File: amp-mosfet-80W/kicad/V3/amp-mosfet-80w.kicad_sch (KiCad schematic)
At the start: 66 parts, among them J1 Conn_01x01, J2 Conn_01x01, J3 +50V, J4 -50V, J5 LS+, J6 LS-, J7 GND, Q1 BC856BS, Q11 ECX10P20, Q12 ECX10N20, Q2 BC856BS, Q3 BC856BS, Q4 BC846BDW1, Q5 DZT5401, Q6 DZT5551, Q7 BC856B, Q8 BC846

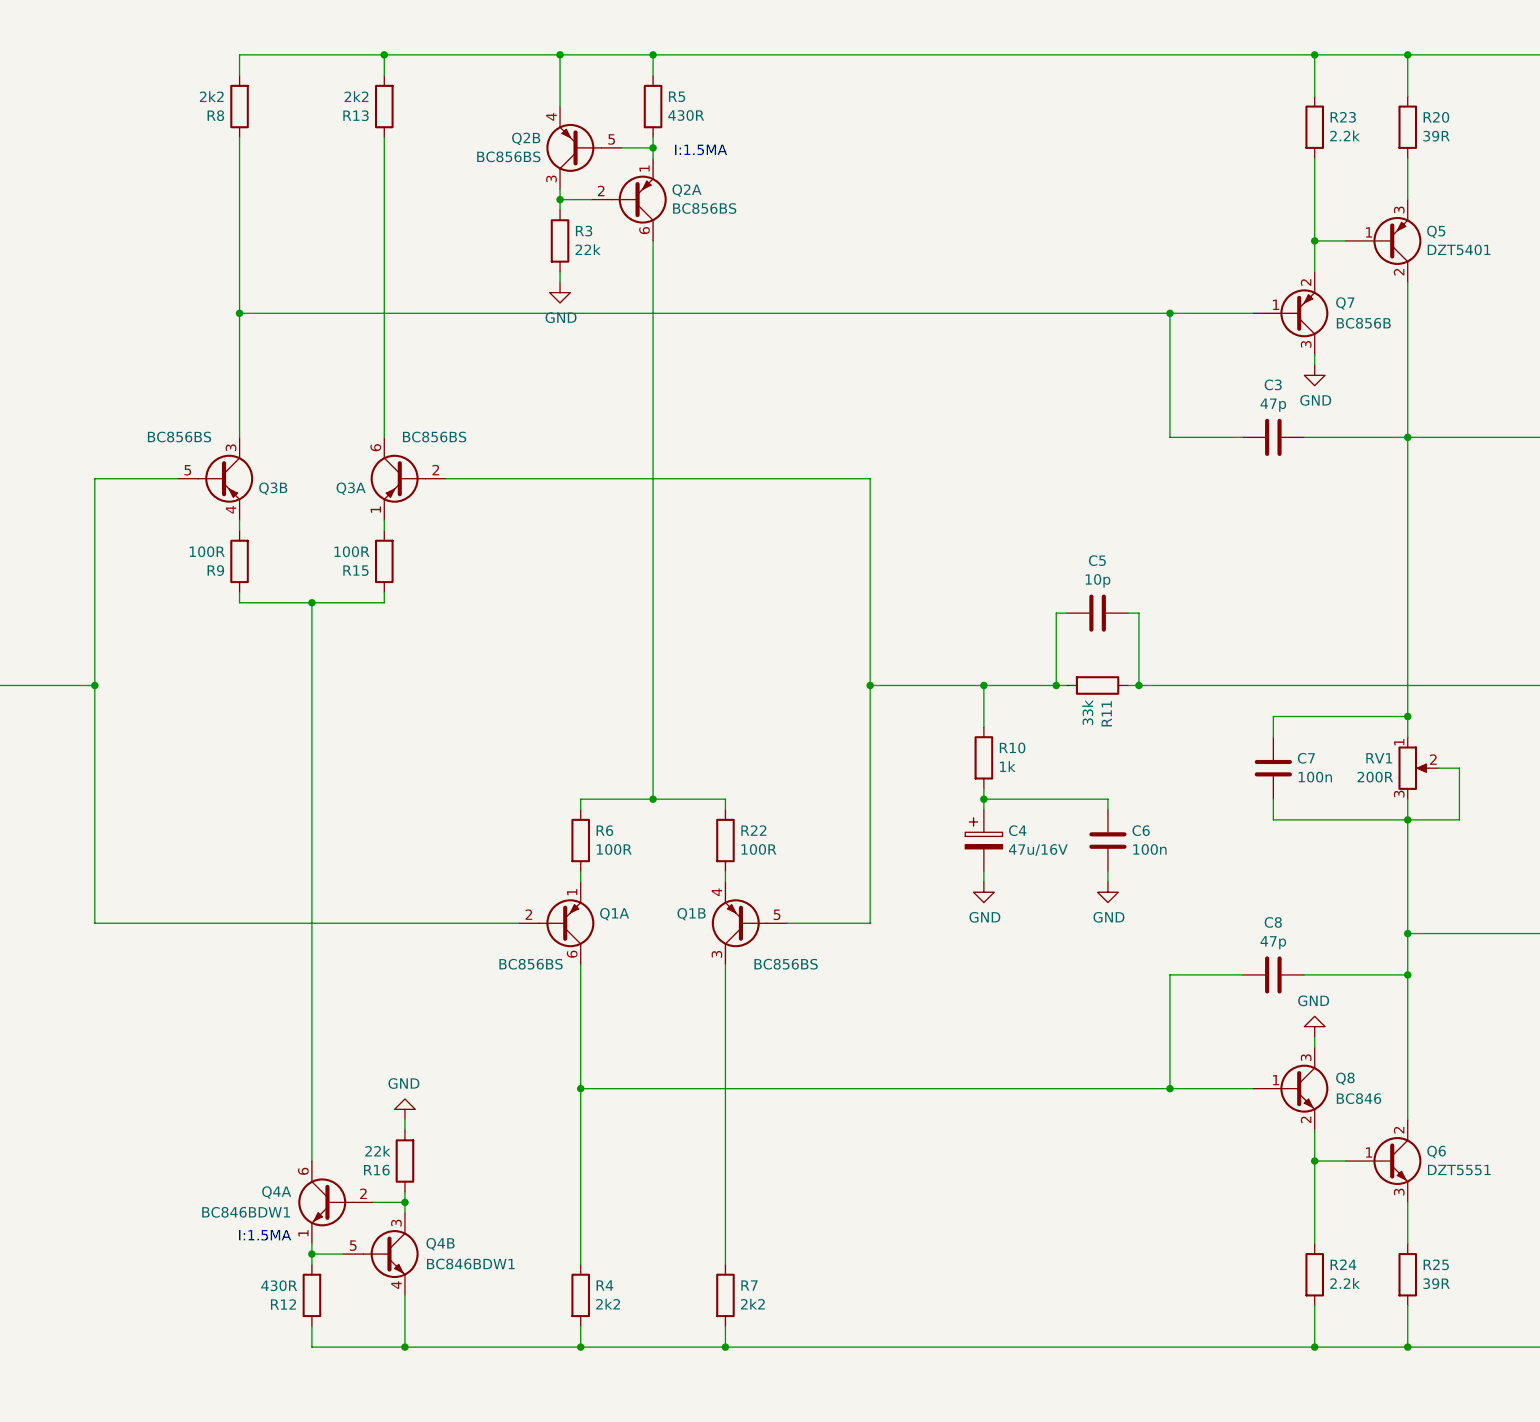
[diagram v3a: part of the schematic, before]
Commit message: Update amp-mosfet-80w.kicad_sch
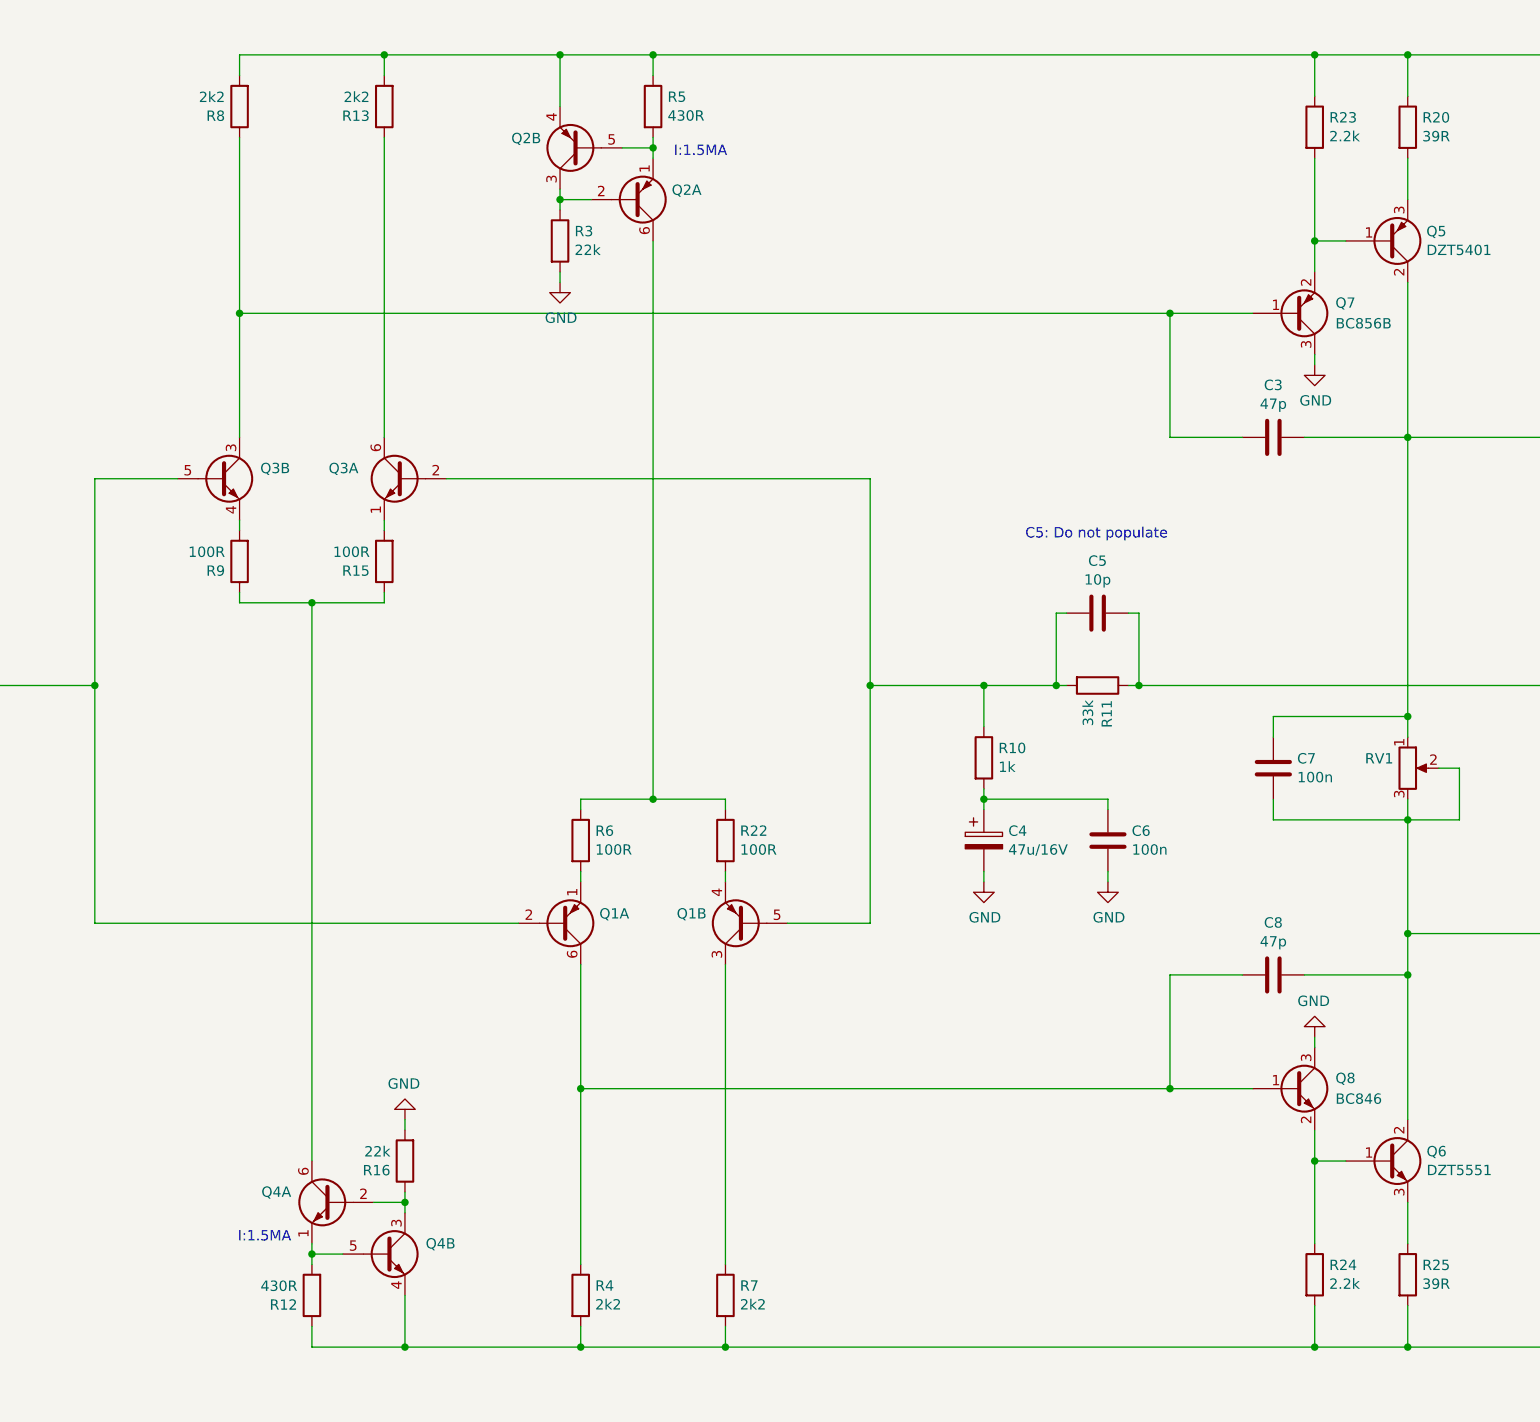
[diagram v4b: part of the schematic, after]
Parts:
- removed Q3: BC856BS, Package_TO_SOT_SMD:SOT-363_SC-70-6, symbol Transistor_BJT:BC856BS
- added Q3: (no value), Package_TO_SOT_SMD:SOT-363_SC-70-6, symbol Transistor_BJT:BC846BDW1
- Q1, Q2: value BC856BS -> (none)
- Q4: value BC846BDW1 -> (none)
- RV1: value 200R -> (none)
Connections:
- net at C2.1, Q1.2 (B1), R2.1: now also Q3.5 (B2)
- net at C5.2, Q1.5 (B2), R10.1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: now also Q3.2 (B1)
- net at R15.2: now also Q3.1 (E1)
- net at R13.1: now also Q3.6 (C1)
- net at C3.2, Q7.1 (B), R8.1: now also Q3.3 (C2)
- net at R9.2: now also Q3.4 (E2)
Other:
- note added: "C5: Do not populate"

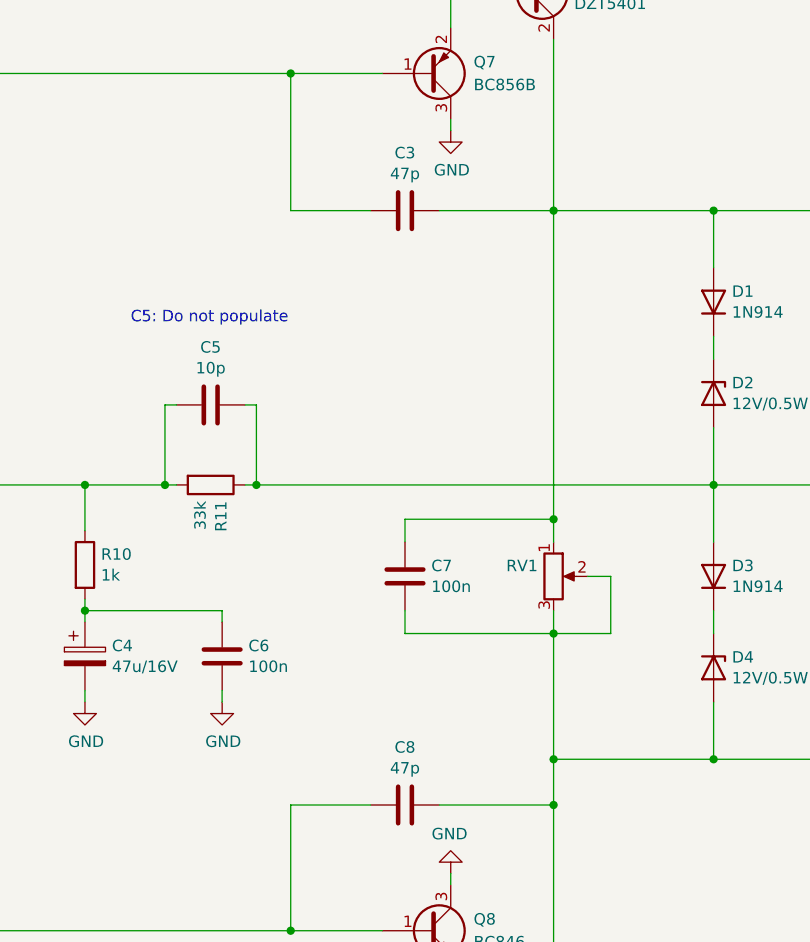
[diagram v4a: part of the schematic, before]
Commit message: Update amp-mosfet-80w.kicad_sch
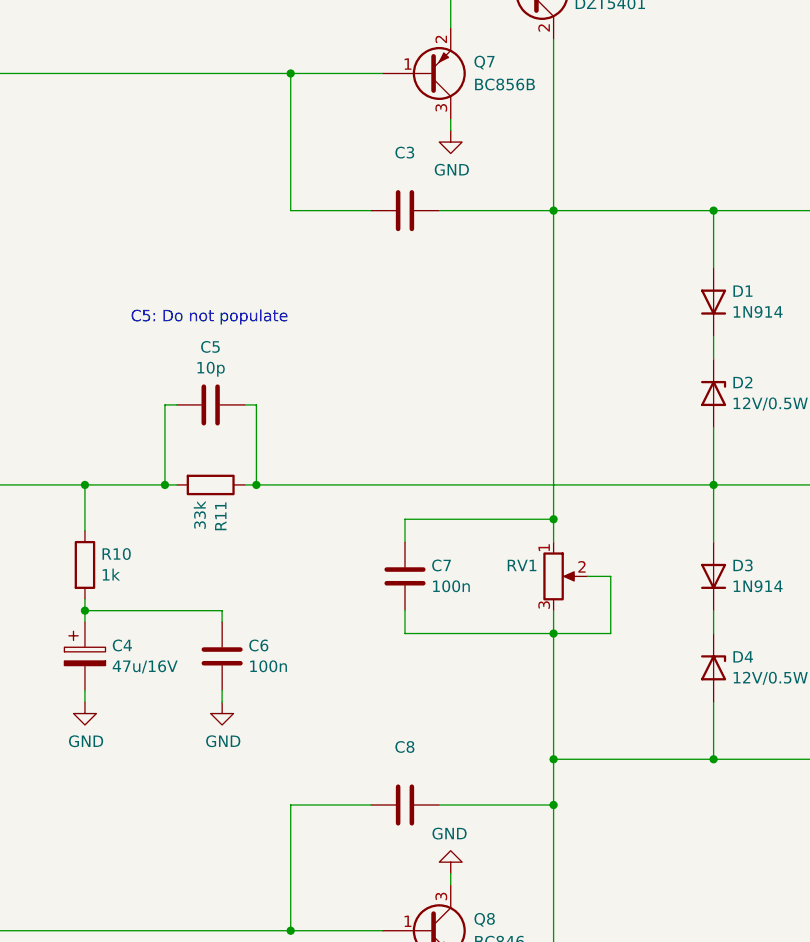
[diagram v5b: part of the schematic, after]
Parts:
- C3, C8: value 47p -> (none)
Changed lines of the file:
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@@
     (in_bom yes) (on_board yes)
     (property "Reference" "C8" (id 0) (at 232.41 165.0492 90))
-    (property "Value" "47p" (id 1) (at 232.41 167.3606 90))
+    (property "Value" "" (id 1) (at 232.41 167.3606 90))
     (property "Footprint" "Capacitor_SMD:C_0805_2012Metric_Pad1.18x1.45mm_HandSolder" (id 2) (at 228.6 172.4152 0)
       (effects (font (size 1.27 1.27)) hide)
@@
     (in_bom yes) (on_board yes)
     (property "Reference" "C3" (id 0) (at 232.41 99.0092 90))
-    (property "Value" "47p" (id 1) (at 232.41 101.3206 90))
+    (property "Value" "" (id 1) (at 232.41 101.3206 90))
     (property "Footprint" "Capacitor_SMD:C_0805_2012Metric_Pad1.18x1.45mm_HandSolder" (id 2) (at 228.6 106.3752 0)
       (effects (font (size 1.27 1.27)) hide)
@@
     )
     (path "/32c5d5f3-0c0f-40b4-a908-6234ed6f8352"
-      (reference "C3") (unit 1) (value "47p") (footprint "Capacitor_SMD:C_0805_2012Metric_Pad1.18x1.45mm_HandSolder")
+      (reference "C3") (unit 1) (value "18p") (footprint "Capacitor_SMD:C_0805_2012Metric_Pad1.18x1.45mm_HandSolder")
     )
     (path "/00000000-0000-0000-0000-00006192b71c"
@@
     )
     (path "/0785ac03-05c0-4141-b336-e53ca306152b"
-      (reference "C8") (unit 1) (value "47p") (footprint "Capacitor_SMD:C_0805_2012Metric_Pad1.18x1.45mm_HandSolder")
+      (reference "C8") (unit 1) (value "18p") (footprint "Capacitor_SMD:C_0805_2012Metric_Pad1.18x1.45mm_HandSolder")
     )
     (path "/00000000-0000-0000-0000-0000619669cb"
